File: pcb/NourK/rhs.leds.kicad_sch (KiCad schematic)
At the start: 43 parts

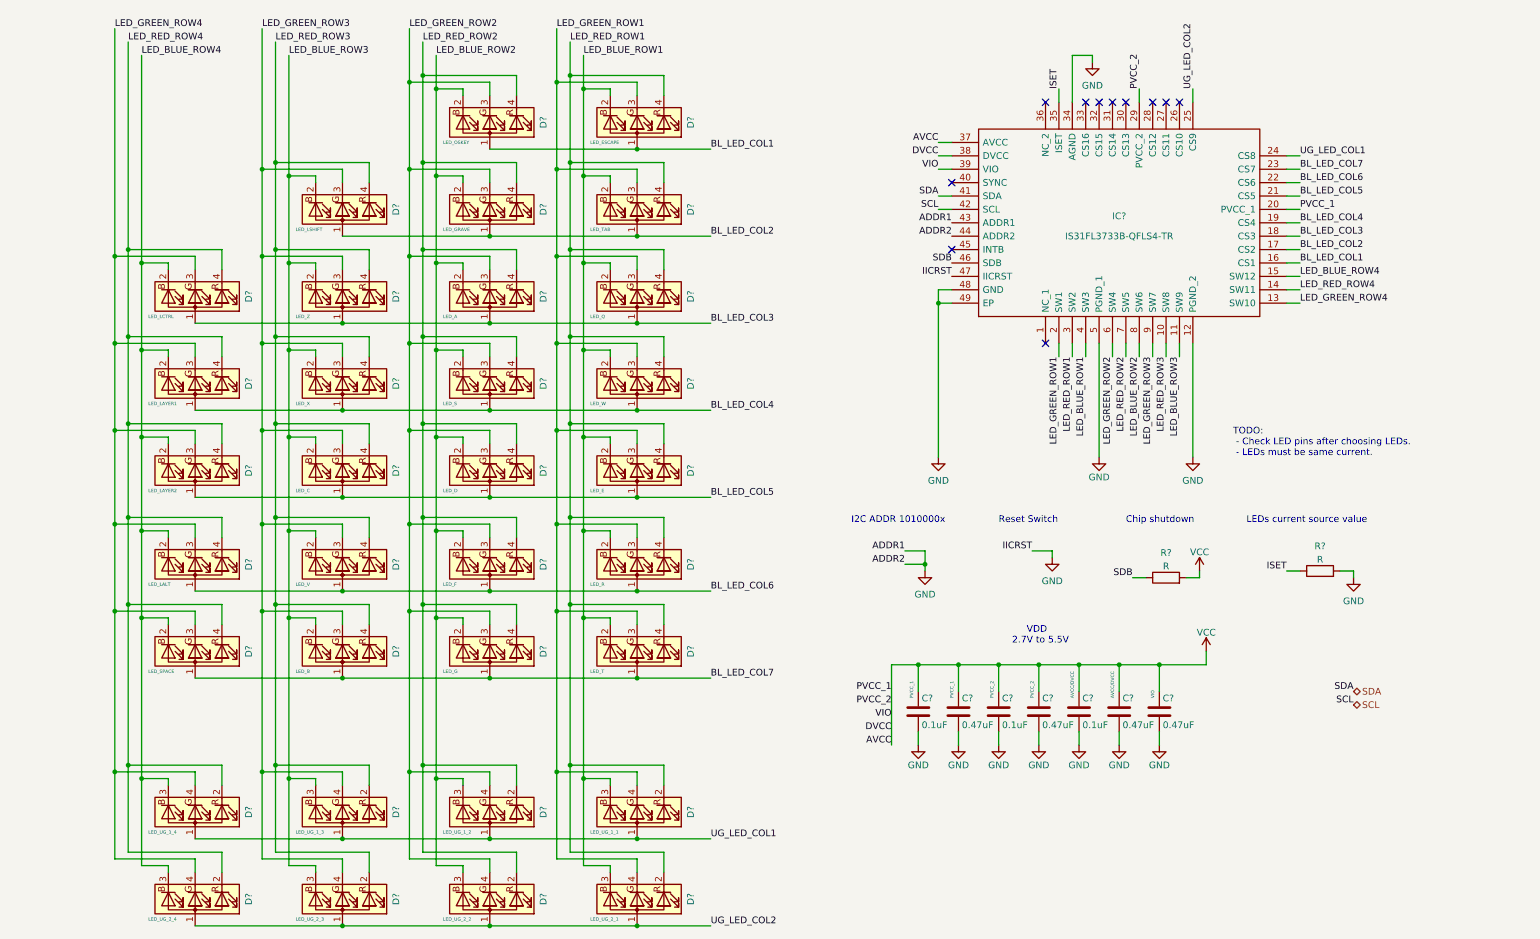
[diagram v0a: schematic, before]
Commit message: Add RHS schematics sheets
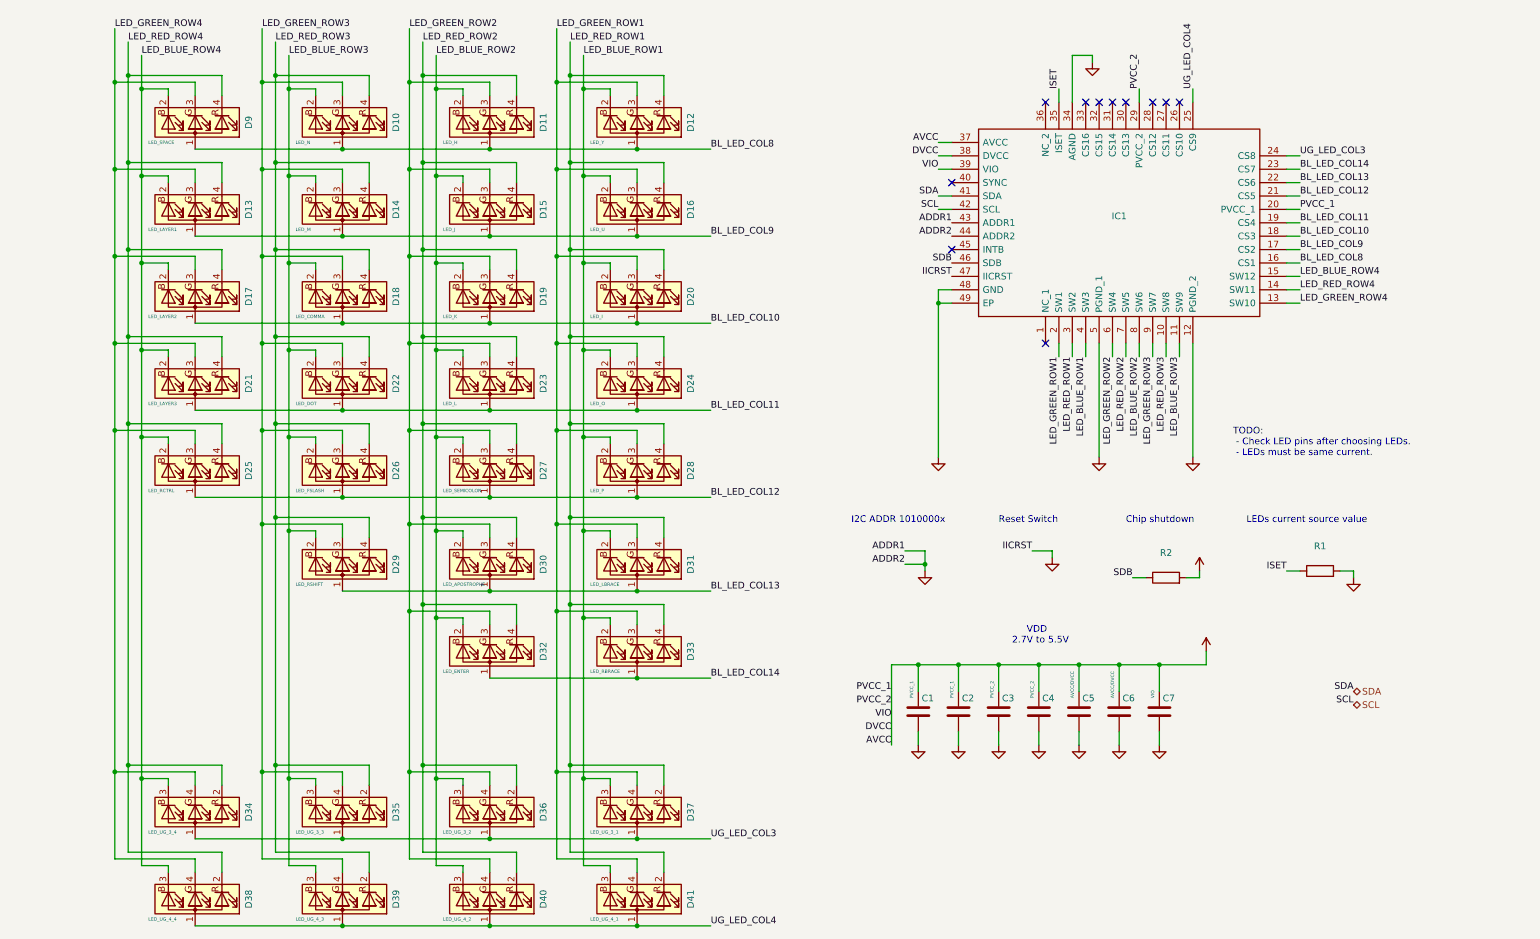
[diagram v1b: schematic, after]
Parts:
- removed C? (x3): 0.1uF, Capacitor_SMD:C_0805_2012Metric, symbol Device:C
- removed C? (x4): 0.47uF, Capacitor_SMD:C_0805_2012Metric, symbol Device:C
- removed D?: LED_LCTRL, Nour_KB:155124M173200, symbol Device:LED_ABGR
- removed D?: LED_SPACE, Nour_KB:155124M173200, symbol Device:LED_ABGR
- removed D?: LED_LALT, Nour_KB:155124M173200, symbol Device:LED_ABGR
- removed D?: LED_UG_2_2, Nour_KB:LTRBR37G4R4S012502R18, symbol Device:LED_ARBG
- removed D?: LED_E, Nour_KB:155124M173200, symbol Device:LED_ABGR
- removed D?: LED_LAYER1, Nour_KB:155124M173200, symbol Device:LED_ABGR
- removed D?: LED_C, Nour_KB:155124M173200, symbol Device:LED_ABGR
- removed D?: LED_UG_1_1, Nour_KB:LTRBR37G4R4S012502R18, symbol Device:LED_ARBG
- removed D?: LED_F, Nour_KB:155124M173200, symbol Device:LED_ABGR
- removed D?: LED_R, Nour_KB:155124M173200, symbol Device:LED_ABGR
- removed D?: LED_UG_2_4, Nour_KB:LTRBR37G4R4S012502R18, symbol Device:LED_ARBG
- removed D?: LED_V, Nour_KB:155124M173200, symbol Device:LED_ABGR
- removed D?: LED_UG_2_1, Nour_KB:LTRBR37G4R4S012502R18, symbol Device:LED_ARBG
- removed D?: LED_UG_1_3, Nour_KB:LTRBR37G4R4S012502R18, symbol Device:LED_ARBG
- removed D?: LED_ESCAPE, Nour_KB:155124M173200, symbol Device:LED_ABGR
- removed D?: LED_UG_1_4, Nour_KB:LTRBR37G4R4S012502R18, symbol Device:LED_ARBG
- removed D?: LED_D, Nour_KB:155124M173200, symbol Device:LED_ABGR
- removed D?: LED_UG_2_3, Nour_KB:LTRBR37G4R4S012502R18, symbol Device:LED_ARBG
- removed D?: LED_B, Nour_KB:155124M173200, symbol Device:LED_ABGR
- removed D?: LED_UG_1_2, Nour_KB:LTRBR37G4R4S012502R18, symbol Device:LED_ARBG
- removed D?: LED_LAYER2, Nour_KB:155124M173200, symbol Device:LED_ABGR
- removed D?: LED_Q, Nour_KB:155124M173200, symbol Device:LED_ABGR
- removed D?: LED_TAB, Nour_KB:155124M173200, symbol Device:LED_ABGR
- removed D?: LED_S, Nour_KB:155124M173200, symbol Device:LED_ABGR
- removed D?: LED_OSKEY, Nour_KB:155124M173200, symbol Device:LED_ABGR
- removed D?: LED_W, Nour_KB:155124M173200, symbol Device:LED_ABGR
- removed D?: LED_GRAVE, Nour_KB:155124M173200, symbol Device:LED_ABGR
- removed D?: LED_G, Nour_KB:155124M173200, symbol Device:LED_ABGR
- removed D?: LED_LSHIFT, Nour_KB:155124M173200, symbol Device:LED_ABGR
- removed D?: LED_T, Nour_KB:155124M173200, symbol Device:LED_ABGR
- removed D?: LED_Z, Nour_KB:155124M173200, symbol Device:LED_ABGR
- removed D?: LED_X, Nour_KB:155124M173200, symbol Device:LED_ABGR
- removed D?: LED_A, Nour_KB:155124M173200, symbol Device:LED_ABGR
- removed IC?: IS31FL3733B-QFLS4-TR, Nour_KB:QFN40P600X600X80-49N-D, symbol Nour_KB:IS31FL3733B-QFLS4-TR
- removed R? (x2): R, Resistor_SMD:R_0805_2012Metric, symbol Device:R
- added C1, C2, C3, C4, C5, C6, C7: (no value), symbol Device:C
- added D10: LED_N, symbol Device:LED_ABGR
- added D11: LED_H, symbol Device:LED_ABGR
- added D12: LED_Y, symbol Device:LED_ABGR
- added D13: LED_LAYER1, symbol Device:LED_ABGR
- added D14: LED_M, symbol Device:LED_ABGR
- added D15: LED_J, symbol Device:LED_ABGR
- added D16: LED_U, symbol Device:LED_ABGR
- added D17: LED_LAYER2, symbol Device:LED_ABGR
- added D18: LED_COMMA, symbol Device:LED_ABGR
- added D19: LED_K, symbol Device:LED_ABGR
- added D20: LED_I, symbol Device:LED_ABGR
- added D21: LED_LAYER3, symbol Device:LED_ABGR
- added D22: LED_DOT, symbol Device:LED_ABGR
- added D23: LED_L, symbol Device:LED_ABGR
- added D24: LED_O, symbol Device:LED_ABGR
- added D25: LED_RCTRL, symbol Device:LED_ABGR
- added D26: LED_FSLASH, symbol Device:LED_ABGR
- added D27: LED_SEMICOLON, symbol Device:LED_ABGR
- added D28: LED_P, symbol Device:LED_ABGR
- added D29: LED_RSHIFT, symbol Device:LED_ABGR
- added D30: LED_APOSTROPHE, symbol Device:LED_ABGR
- added D31: LED_LBRACE, symbol Device:LED_ABGR
- added D32: LED_ENTER, symbol Device:LED_ABGR
- added D33: LED_RBRACE, symbol Device:LED_ABGR
- added D34: LED_UG_3_4, symbol Device:LED_ARBG
- added D35: LED_UG_3_3, symbol Device:LED_ARBG
- added D36: LED_UG_3_2, symbol Device:LED_ARBG
- added D37: LED_UG_3_1, symbol Device:LED_ARBG
- added D38: LED_UG_4_4, symbol Device:LED_ARBG
- added D39: LED_UG_4_3, symbol Device:LED_ARBG
- added D40: LED_UG_4_2, symbol Device:LED_ARBG
- added D41: LED_UG_4_1, symbol Device:LED_ARBG
- added D9: LED_SPACE, symbol Device:LED_ABGR
- added IC1: (no value), symbol Nour_KB:IS31FL3733B-QFLS4-TR
- added R1, R2: (no value), symbol Device:R
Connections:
- net GND: now also C1.2, C2.2, C3.2, C4.2, C5.2, C6.2, C7.2, IC1.12 (PGND_2), IC1.34 (AGND), IC1.43 (ADDR1), IC1.44 (ADDR2), IC1.47 (IICRST), IC1.48 (GND), IC1.49 (EP), IC1.5 (PGND_1), R1.2
- net ISET: now also IC1.35 (ISET), R1.1
- net LED_BLUE_ROW1: now also D12.2 (BK), D16.2 (BK), D20.2 (BK), D24.2 (BK), D28.2 (BK), D31.2 (BK), D33.2 (BK), D37.3 (BK), D41.3 (BK), IC1.4 (SW3)
- net LED_BLUE_ROW2: now also D11.2 (BK), D15.2 (BK), D19.2 (BK), D23.2 (BK), D27.2 (BK), D30.2 (BK), D32.2 (BK), D36.3 (BK), D40.3 (BK), IC1.8 (SW6)
- net LED_BLUE_ROW3: now also D10.2 (BK), D14.2 (BK), D18.2 (BK), D22.2 (BK), D26.2 (BK), D29.2 (BK), D35.3 (BK), D39.3 (BK), IC1.11 (SW9)
- net LED_BLUE_ROW4: now also D13.2 (BK), D17.2 (BK), D21.2 (BK), D25.2 (BK), D34.3 (BK), D38.3 (BK), D9.2 (BK), IC1.15 (SW12)
- net LED_GREEN_ROW1: now also D12.3 (GK), D16.3 (GK), D20.3 (GK), D24.3 (GK), D28.3 (GK), D31.3 (GK), D33.3 (GK), D37.4 (GK), D41.4 (GK), IC1.2 (SW1)
- net LED_GREEN_ROW2: now also D11.3 (GK), D15.3 (GK), D19.3 (GK), D23.3 (GK), D27.3 (GK), D30.3 (GK), D32.3 (GK), D36.4 (GK), D40.4 (GK), IC1.6 (SW4)
- net LED_GREEN_ROW3: now also D10.3 (GK), D14.3 (GK), D18.3 (GK), D22.3 (GK), D26.3 (GK), D29.3 (GK), D35.4 (GK), D39.4 (GK), IC1.9 (SW7)
- net LED_GREEN_ROW4: now also D13.3 (GK), D17.3 (GK), D21.3 (GK), D25.3 (GK), D34.4 (GK), D38.4 (GK), D9.3 (GK), IC1.13 (SW10)
- net LED_RED_ROW1: now also D12.4 (RK), D16.4 (RK), D20.4 (RK), D24.4 (RK), D28.4 (RK), D31.4 (RK), D33.4 (RK), D37.2 (RK), D41.2 (RK), IC1.3 (SW2)
- net LED_RED_ROW2: now also D11.4 (RK), D15.4 (RK), D19.4 (RK), D23.4 (RK), D27.4 (RK), D30.4 (RK), D32.4 (RK), D36.2 (RK), D40.2 (RK), IC1.7 (SW5)
- net LED_RED_ROW3: now also D10.4 (RK), D14.4 (RK), D18.4 (RK), D22.4 (RK), D26.4 (RK), D29.4 (RK), D35.2 (RK), D39.2 (RK), IC1.10 (SW8)
- net LED_RED_ROW4: now also D13.4 (RK), D17.4 (RK), D21.4 (RK), D25.4 (RK), D34.2 (RK), D38.2 (RK), D9.4 (RK), IC1.14 (SW11)
- net SCL: now also IC1.42 (SCL)
- net SDA: now also IC1.41 (SDA)
- net SDB: now also IC1.46 (SDB), R2.1
- net VCC: now also C1.1, C2.1, C3.1, C4.1, C5.1, C6.1, C7.1, IC1.20 (PVCC_1), IC1.29 (PVCC_2), IC1.37 (AVCC), IC1.38 (DVCC), IC1.39 (VIO), R2.2
- new net BL_LED_COL10: D17.1 (A), D18.1 (A), D19.1 (A), D20.1 (A), IC1.18 (CS3)
- new net BL_LED_COL11: D21.1 (A), D22.1 (A), D23.1 (A), D24.1 (A), IC1.19 (CS4)
- new net BL_LED_COL12: D25.1 (A), D26.1 (A), D27.1 (A), D28.1 (A), IC1.21 (CS5)
- new net BL_LED_COL13: D29.1 (A), D30.1 (A), D31.1 (A), IC1.22 (CS6)
- new net BL_LED_COL14: D32.1 (A), D33.1 (A), IC1.23 (CS7)
- new net BL_LED_COL8: D10.1 (A), D11.1 (A), D12.1 (A), D9.1 (A), IC1.16 (CS1)
- new net BL_LED_COL9: D13.1 (A), D14.1 (A), D15.1 (A), D16.1 (A), IC1.17 (CS2)
- new net UG_LED_COL3: D34.1 (A), D35.1 (A), D36.1 (A), D37.1 (A), IC1.24 (CS8)
- new net UG_LED_COL4: D38.1 (A), D39.1 (A), D40.1 (A), D41.1 (A), IC1.25 (CS9)

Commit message: Draft LHS tracks
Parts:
- removed C1, C2, C3, C4, C5, C6, C7: (no value), symbol Device:C
- removed IC1: (no value), symbol Nour_KB:IS31FL3733B-QFLS4-TR
- removed R1, R2: (no value), symbol Device:R
- D10: renamed from D11; footprint (none) -> Nour_KB:155124M173200
- D11: renamed from D10; footprint (none) -> Nour_KB:155124M173200
- D12: renamed from D9; footprint (none) -> Nour_KB:155124M173200
- D13: renamed from D16; footprint (none) -> Nour_KB:155124M173200
- D14: renamed from D15; footprint (none) -> Nour_KB:155124M173200
- D15: renamed from D14; footprint (none) -> Nour_KB:155124M173200
- D16: renamed from D13; footprint (none) -> Nour_KB:155124M173200
- D17: renamed from D20; footprint (none) -> Nour_KB:155124M173200
- D18: renamed from D19; footprint (none) -> Nour_KB:155124M173200
- D19: renamed from D18; footprint (none) -> Nour_KB:155124M173200
- D20: renamed from D17; footprint (none) -> Nour_KB:155124M173200
- D21: renamed from D24; footprint (none) -> Nour_KB:155124M173200
- D22: renamed from D23; footprint (none) -> Nour_KB:155124M173200
- D23: renamed from D22; footprint (none) -> Nour_KB:155124M173200
- D24: renamed from D21; footprint (none) -> Nour_KB:155124M173200
- D25: renamed from D28; footprint (none) -> Nour_KB:155124M173200
- D26: renamed from D27; footprint (none) -> Nour_KB:155124M173200
- D27: renamed from D26; footprint (none) -> Nour_KB:155124M173200
- D28: renamed from D25; footprint (none) -> Nour_KB:155124M173200
- D29: renamed from D31; footprint (none) -> Nour_KB:155124M173200
- D30: footprint (none) -> Nour_KB:155124M173200
- D31: renamed from D29; footprint (none) -> Nour_KB:155124M173200
- D32: renamed from D33; footprint (none) -> Nour_KB:155124M173200
- D33: renamed from D32; footprint (none) -> Nour_KB:155124M173200
- D34: renamed from D37; footprint (none) -> Nour_KB:LTRBR37G4R4S012502R18
- D35: renamed from D36; footprint (none) -> Nour_KB:LTRBR37G4R4S012502R18
- D36: renamed from D35; footprint (none) -> Nour_KB:LTRBR37G4R4S012502R18
- D37: renamed from D34; footprint (none) -> Nour_KB:LTRBR37G4R4S012502R18
- D38: renamed from D41; footprint (none) -> Nour_KB:LTRBR37G4R4S012502R18
- D39: renamed from D40; footprint (none) -> Nour_KB:LTRBR37G4R4S012502R18
- D40: renamed from D39; footprint (none) -> Nour_KB:LTRBR37G4R4S012502R18
- D41: renamed from D38; footprint (none) -> Nour_KB:LTRBR37G4R4S012502R18
- D9: renamed from D12; footprint (none) -> Nour_KB:155124M173200
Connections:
- net BL_LED_COL10 renamed LED.CS_COL3
- net BL_LED_COL11 renamed LED.CS_COL4
- net BL_LED_COL12 renamed LED.CS_COL5
- net BL_LED_COL13 renamed LED.CS_COL6
- net BL_LED_COL14 renamed LED.CS_COL7
- net BL_LED_COL8 renamed LED.CS_COL1
- net BL_LED_COL9 renamed LED.CS_COL2
- net LED_BLUE_ROW1 renamed LED.SW_BLUE1
- net LED_BLUE_ROW2 renamed LED.SW_BLUE2
- net LED_BLUE_ROW3 renamed LED.SW_BLUE3
- net LED_BLUE_ROW4 renamed LED.SW_BLUE4
- net LED_GREEN_ROW1 renamed LED.SW_GREEN1
- net LED_GREEN_ROW2 renamed LED.SW_GREEN2
- net LED_GREEN_ROW3 renamed LED.SW_GREEN3
- net LED_GREEN_ROW4 renamed LED.SW_GREEN4
- net LED_RED_ROW1 renamed LED.SW_RED1
- net LED_RED_ROW2 renamed LED.SW_RED2
- net LED_RED_ROW3 renamed LED.SW_RED3
- net LED_RED_ROW4 renamed LED.SW_RED4
- net UG_LED_COL3 renamed LED.CS_COL8
- net UG_LED_COL4 renamed LED.CS_COL9
- no-connect marks 11 -> 0
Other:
- note removed: "Chip shutdown"
- note removed: "I2C ADDR 1010000x"
- note removed: "LEDs current source value"
- note removed: "Reset Switch"
- note removed: "TODO: - Check LED pins after choosing LEDs. - LEDs must be same current."
- note removed: "VDD 2.7V to 5.5V"
- moved on the sheet: D10, D11, D12, D13, D14, D15, D16, D17, D18, D19, D20, D21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
